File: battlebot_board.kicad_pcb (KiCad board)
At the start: 4 copper layers, 60 x 45 mm, 41 parts, among them J1 Conn_01x02_Pin, J2 Conn_01x04_Pin, J3 JST_SMD_1.0mm_Vertical, J5 JST_02, J6 JST_02, Q1 AO3400A, Q2 AO3400A, SW1 Switch_Tactile_CnK, U1 AP63203WU, U2 LPC824M201JHI33, U3 TMP102, U4 LSM6DSOX, U5 W25Q128JVP

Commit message: added fuses and moved diodes for thermal protection
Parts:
- removed the Ref** at (177.0, 62.0)
- added F1: 16V/2.5A/5.0A, PCM_SparkFun-Fuse:1812, F.Cu at (179.9, 60.5)
- added F2: 16V/2.5A/5.0A, PCM_SparkFun-Fuse:1812, F.Cu at (175.5, 60.5)
- added F3: 16V/2.5A/5.0A, PCM_SparkFun-Fuse:1812, F.Cu at (171.1, 60.5)
- added Ref**: Val**, PCM_SparkFun-Aesthetic:OSHW_Logo_6mm, F.Cu at (159.0, 73.0)
- moved R1 3.04 mm to (184.0, 88.5)
- moved SW1 3.04 mm to (179.5, 92.0)
- moved D4 1.00 mm to (195.1, 82.0)
- moved D5 1.00 mm to (195.0, 89.5)
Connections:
- C10 pad 1: 12V -> Net-(D4-K)
- C12 pad 1: 12V -> Net-(D4-K)
- D4 pad 1: 12V -> Net-(D4-K)
- D5 pad 1: 12V -> Net-(D4-K)
- J5 pad 2: 12V -> Net-(D4-K)
- J6 pad 2: 12V -> Net-(D4-K)
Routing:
- net Net-(D4-K): track 0.00 -> 58.2 mm, vias 0 -> 5
- net 12V: track 90.7 -> 84.1 mm, vias 2 -> 0
- net /NRST: track 31.5 -> 29.8 mm
- net Net-(D5-A): track 54.6 -> 55.6 mm

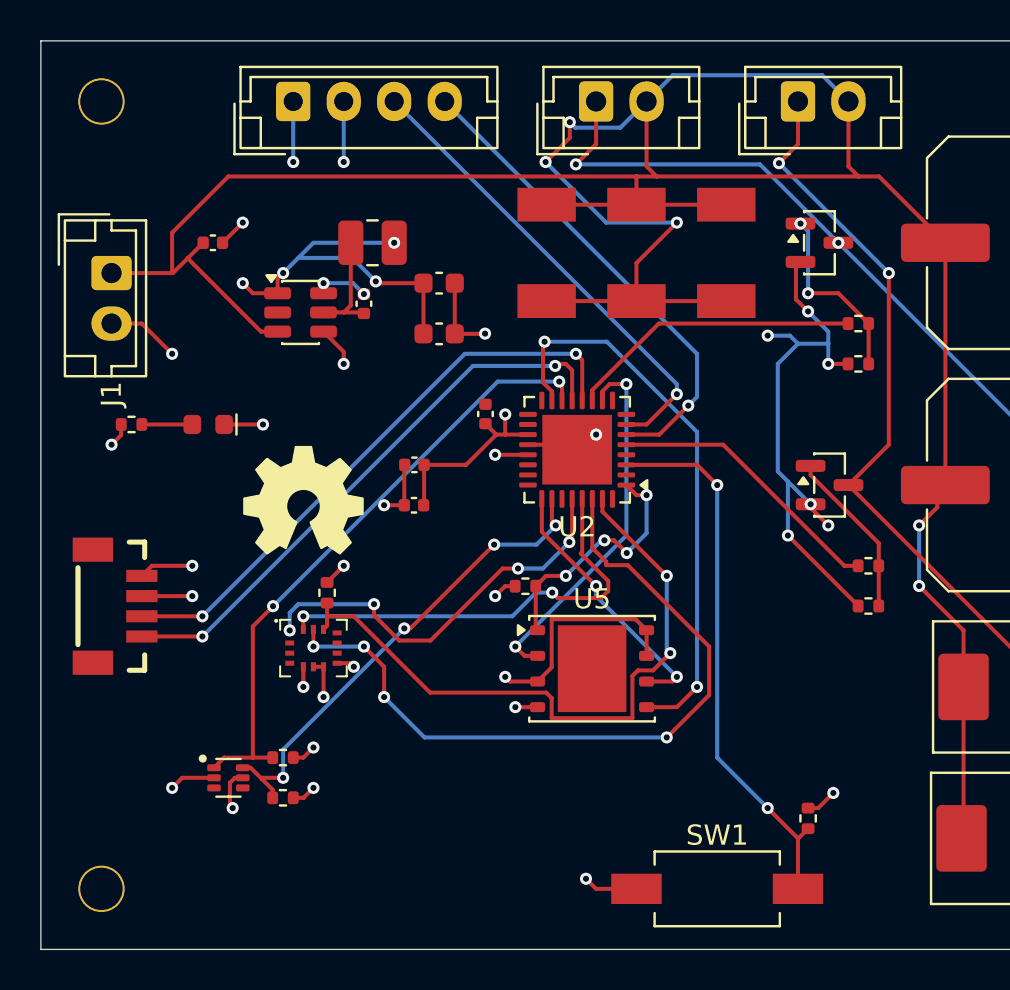
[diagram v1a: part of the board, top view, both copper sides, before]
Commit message: replaced parallel fuses with fuse blade holder
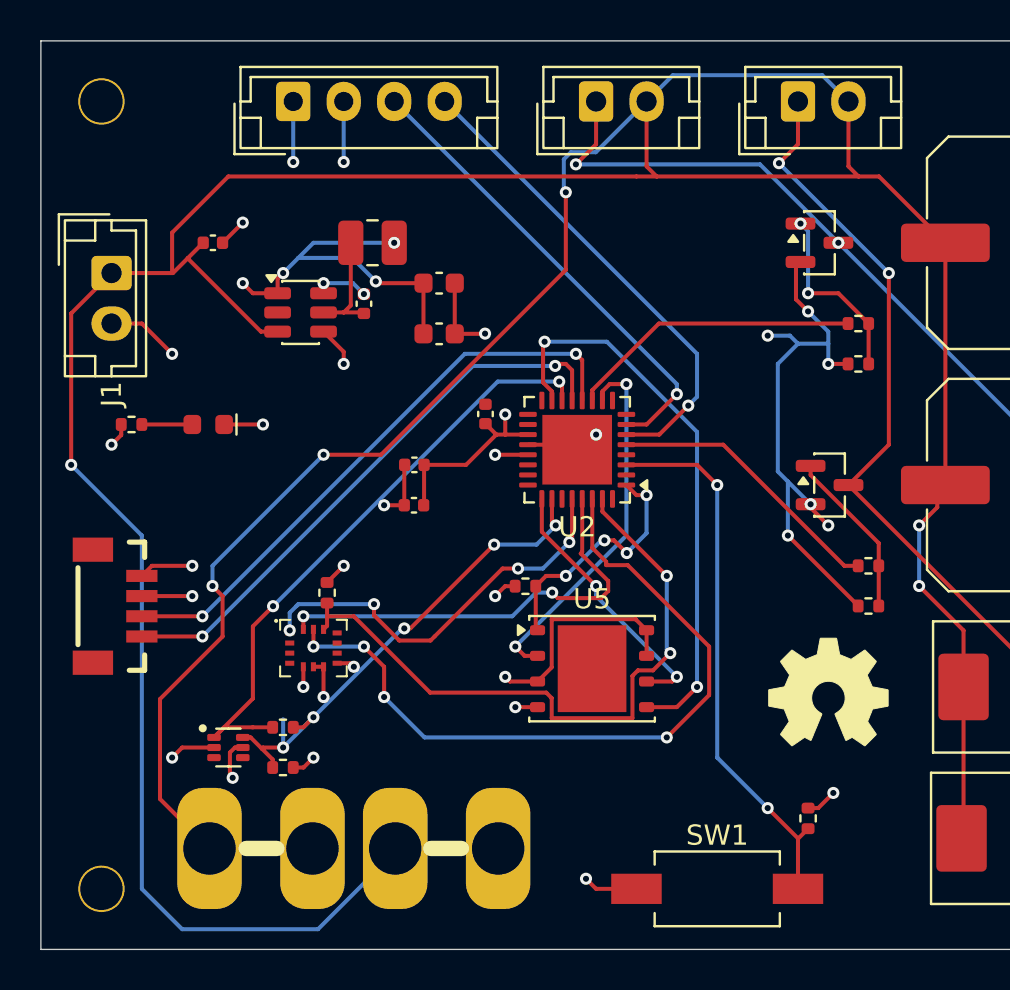
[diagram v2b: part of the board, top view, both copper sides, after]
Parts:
- removed F1, F2, F3: 16V/2.5A/5.0A, PCM_SparkFun-Fuse:1812
- added F4: Blade Fuse, PCM_SparkFun-Fuse:Fuseholder_Automotive, F.Cu at (161.5, 90.0)
- moved Ref** 27.7 mm to (185.0, 82.5)
- moved R4 1.50 mm to (158.0, 84.0)
- moved R5 1.50 mm to (158.0, 86.0)
- moved U3 1.50 mm to (155.3, 85.0)
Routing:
- net 12V: track 84.1 -> 126.8 mm, vias 0 -> 1
- net Net-(D4-K): track 58.2 -> 85.9 mm

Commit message: expose I2C1, fix power delivery wiring, and change credits
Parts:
- added J4: Conn_01x02, Connector_JST:JST_EH_B2B-EH-A_1x02_P2.50mm_Vertical, F.Cu at (148.2, 87.2)
- moved J5 10.0 mm to (183.5, 53.0)
- moved J6 9.50 mm to (174.0, 53.0)
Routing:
- net 12V: track 126.8 -> 64.1 mm
- net Net-(D4-K): track 85.9 -> 106.9 mm
- net Net-(D5-A): track 55.6 -> 45.2 mm, vias 3 -> 2
- net /SCL1: track 30.6 -> 40.8 mm, vias 2 -> 4
- net /SDA1: track 24.3 -> 34.3 mm, vias 4 -> 5
- net Net-(D4-A): track 39.2 -> 45.9 mm, vias 2 -> 3
- net GND: track 70.5 -> 71.6 mm, vias 21 -> 22
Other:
- board text added: "Designed by Benjamin Liu"
- board text removed: "Designed by Benjamin Liu With help from Leo Nguyen"

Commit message: logos and housekeeping
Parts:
- added G***: LOGO, LOGO, B.Cu at (160.5, 112.0)
- moved C2 41.4 mm to (127.0, 91.0)
- moved R10 41.4 mm to (123.0, 100.0)
- moved C1 41.4 mm to (137.0, 102.0)
- moved C10 41.4 mm to (167.7, 91.0)
- moved C12 41.4 mm to (167.7, 103.0)
- moved C4 41.4 mm to (138.2, 93.0)
- moved C5 41.4 mm to (138.2, 95.5)
- moved C7 41.4 mm to (140.5, 99.5)
- moved C8 41.4 mm to (137.0, 104.0)
- moved D3 41.4 mm to (126.8, 100.0)
- moved D4 41.4 mm to (167.6, 113.0)
- moved D5 41.4 mm to (167.5, 120.5)
- moved F4 41.4 mm to (134.0, 121.0)
- moved H1 41.4 mm to (121.5, 84.0)
- moved H2 41.4 mm to (175.5, 84.0)
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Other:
- board text added: "SDA SCL"

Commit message: fixes
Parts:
- moved J3 2.55 mm to (121.5, 106.5)
- moved J4 1.76 mm to (120.5, 116.5)
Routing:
- net 3.3V: track 57.8 -> 53.7 mm
- net 12V: track 64.1 -> 66.1 mm
- net Net-(D4-A): track 45.9 -> 47.2 mm, vias 3 -> 5
- net /SDA1: track 34.3 -> 35.4 mm
- net /SCL1: track 40.8 -> 40.1 mm
- net /TXD: track 28.5 -> 28.0 mm
- net /RXD: track 29.3 -> 28.8 mm

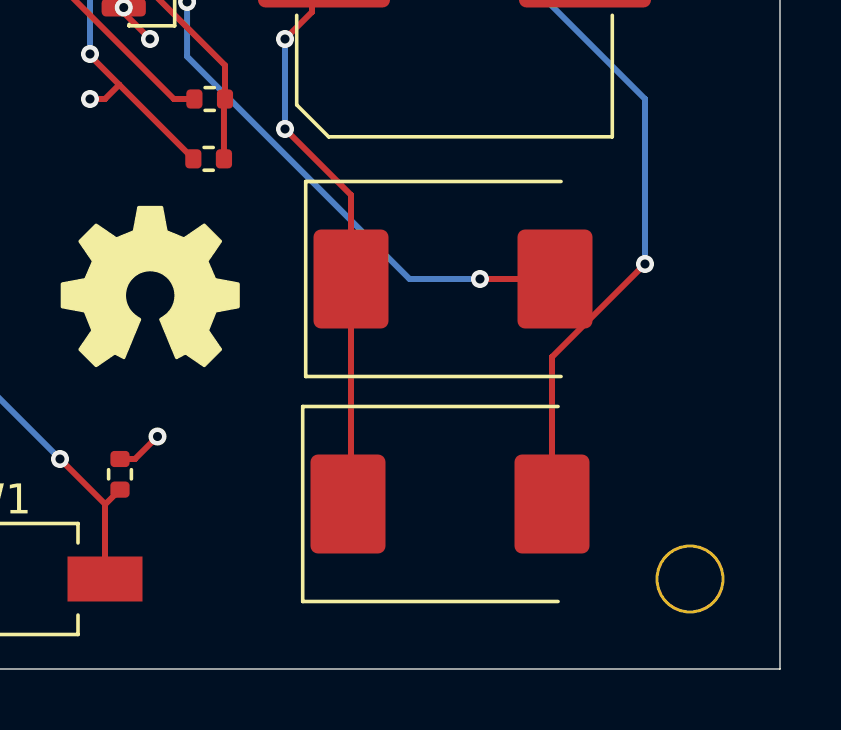
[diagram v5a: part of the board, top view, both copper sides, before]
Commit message: stitching vias
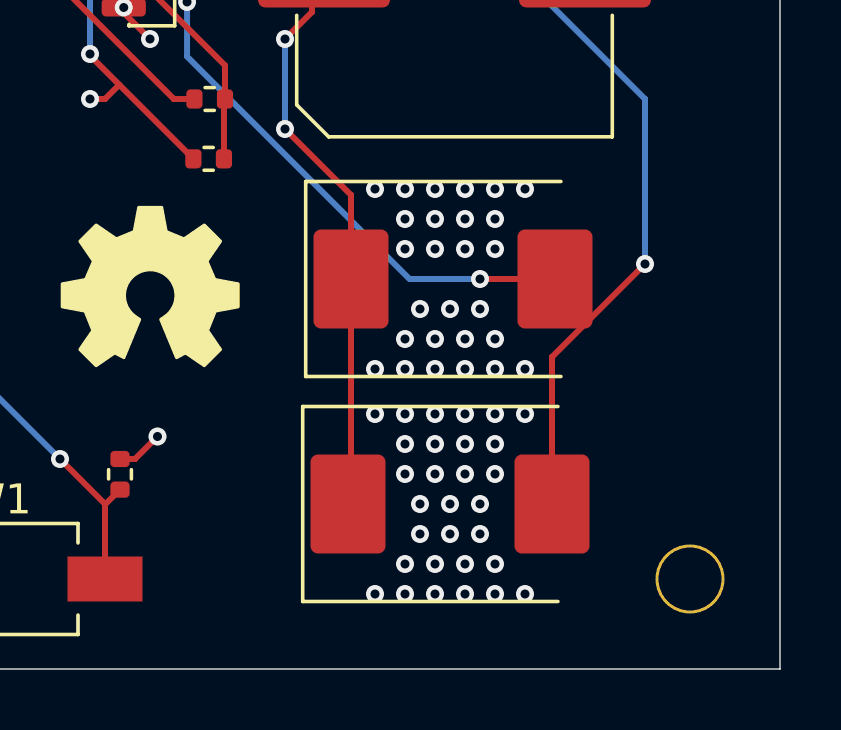
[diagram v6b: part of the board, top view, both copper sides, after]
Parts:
- moved G*** 5.52 mm to (155.0, 111.5)
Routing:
- net (no net): vias 0 -> 57

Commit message: redesign
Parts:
- removed D3: Green, PCM_SparkFun-LED:LED_0603_1608Metric_Green
- removed D4, D5: B340, Diode_SMD:D_SMC
- removed F4: Blade Fuse, PCM_SparkFun-Fuse:Fuseholder_Automotive
- removed G***: LOGO, LOGO
- removed H1, H2, H3, H4: ~, PCM_fab:MountingHole_M2
- removed Q1, Q2: AO3400A, Package_TO_SOT_SMD:SOT-23
- removed R10, R7, R9: 10k, PCM_SparkFun-Resistor:R_0402_1005Metric
- removed R8: 100, PCM_SparkFun-Resistor:R_0402_1005Metric
- removed Ref**: Val**, PCM_SparkFun-Aesthetic:OSHW_Logo_6mm
- removed SW1: Switch_Tactile_CnK, PCM_fab:Button_CnK_PTS636.0_6x3.5mm
- added C11: 0.1uF, PCM_SparkFun-Capacitor:C_0402_1005Metric, F.Cu at (146.5, 97.0)
- added C13: 470uF, PCM_SparkFun-Capacitor:Electrolytic_10.3x10.3mm, F.Cu at (177.2, 100.0)
- added C14: 0.1uF, PCM_SparkFun-Capacitor:C_0402_1005Metric, F.Cu at (155.3, 114.0)
- added C15: 1.0uF, PCM_SparkFun-Capacitor:C_0402_1005Metric, F.Cu at (147.1, 116.5)
- added C6: 0.1uF, PCM_SparkFun-Capacitor:C_0402_1005Metric, F.Cu at (162.0, 99.2)
- added C9: 10nF, PCM_SparkFun-Capacitor:C_0402_1005Metric, F.Cu at (162.2, 103.5)
- added D1: Green, PCM_SparkFun-LED:LED_0603_1608Metric_Green, F.Cu at (128.3, 105.6)
- added D2: PMEG4005EJ, Diode_SMD:D_SOD-323F, F.Cu at (148.0, 114.7)
- added F1: 16V/2.5A/5.0A, PCM_SparkFun-Fuse:1812, F.Cu at (139.0, 76.8)
- added J7: Conn_02x03, Connector_PinHeader_1.27mm:PinHeader_2x03_P1.27mm_Vertical, F.Cu at (137.2, 115.9)
- added L2: 600 Ohm, PCM_SparkFun-Capacitor:C_0805_2012Metric, F.Cu at (159.0, 104.2)
- added L3: 10uH, PCM_SparkFun-Capacitor:C_0805_2012Metric, F.Cu at (151.5, 113.2)
- added REF**: MountingHole_2.2mm_M2_DIN965, MountingHole:MountingHole_2.2mm_M2_DIN965, F.Cu at (128.2, 115.2)
- added REF**: MountingHole_2.2mm_M2_DIN965, MountingHole:MountingHole_2.2mm_M2_DIN965, F.Cu at (181.8, 76.8)
- added REF**: MountingHole_2.2mm_M2_DIN965, MountingHole:MountingHole_2.2mm_M2_DIN965, F.Cu at (181.8, 115.2)
- added REF**: MountingHole_2.2mm_M2_DIN965, MountingHole:MountingHole_2.2mm_M2_DIN965, F.Cu at (128.2, 76.8)
- C1, C2: value 10uF -> 0.1uF
- C10: value 470uF -> 0.1uF; footprint PCM_SparkFun-Capacitor:Electrolytic_10.3x10.3mm -> PCM_SparkFun-Capacitor:C_0402_1005Metric
- C3: value 0.1uF -> 22uF; footprint PCM_SparkFun-Capacitor:C_0402_1005Metric -> PCM_SparkFun-Capacitor:C_0603_1608Metric
- C5: value 22uF -> 0.1uF; footprint PCM_SparkFun-Capacitor:C_0603_1608Metric -> PCM_SparkFun-Capacitor:C_0402_1005Metric
- C7: value 0.1uF -> 10uF
- C8: value 0.1uF -> 1.0uF
- J1: value Conn_01x02_Pin -> Conn_01x03_Socket; footprint Connector_JST:JST_EH_B2B-EH-A_1x02_P2.50mm_Vertical -> PCM_SparkFun-Connector:JST_1x03_P1.0mm_Vertical_SMD
- J2: value Conn_01x04_Pin -> Barrel_Jack_SMD; footprint Connector_JST:JST_EH_B4B-EH-A_1x04_P2.50mm_Vertical -> PCM_SparkFun-Connector:Barrel_Jack_SMD
- J3: value JST_SMD_1.0mm_Vertical -> Conn_01x03_Socket; footprint PCM_SparkFun-Connector:JST_1x04_P1.0mm_Vertical_SMD -> PCM_SparkFun-Connector:JST_1x03_P1.0mm_Vertical_SMD
- J4: value Conn_01x02 -> Conn_01x04_Pin; footprint Connector_JST:JST_EH_B2B-EH-A_1x02_P2.50mm_Vertical -> Connector_PinHeader_1.27mm:PinHeader_1x04_P1.27mm_Vertical
- J5: value JST_02 -> Conn_01x04_Socket; footprint Connector_JST:JST_EH_B2B-EH-A_1x02_P2.50mm_Vertical -> PCM_SparkFun-Connector:JST_1x04_P1.0mm_Vertical_SMD
- J6: value JST_02 -> Conn_01x02_Pin; footprint Connector_JST:JST_EH_B2B-EH-A_1x02_P2.50mm_Vertical -> Connector_PinHeader_1.27mm:PinHeader_1x02_P1.27mm_Vertical
- R4, R5: value 4.7k -> 100k
- R6: value 100 -> 33k
- U2: value LPC824M201JHI33 -> LSM6DSOX; footprint Package_DFN_QFN:QFN-32-1EP_5x5mm_P0.5mm_EP3.45x3.45mm -> PCM_SparkFun-Sensor:ST_LGA-14L_2.5x3.0mm_P0.5mm_4x3
- U3: value TMP102 -> W25Q128JVP; footprint PCM_SparkFun-Semiconductor-Standard:SOT-563 -> Package_SON:WSON-8-1EP_6x5mm_P1.27mm_EP3.4x4.3mm
- U4: value LSM6DSOX -> STM32G4A1KEUx; footprint PCM_SparkFun-Sensor:ST_LGA-14L_2.5x3.0mm_P0.5mm_4x3 -> Package_DFN_QFN:QFN-32-1EP_5x5mm_P0.5mm_EP3.45x3.45mm
- U5: value W25Q128JVP -> AP3012; footprint Package_SON:WSON-8-1EP_6x5mm_P1.27mm_EP3.4x4.3mm -> PCM_SparkFun-Semiconductor-Standard:SOT23-5
- moved J4 49.6 mm to (170.1, 115.2)
- moved J1 44.2 mm to (162.0, 73.7), turned to 0 degrees
- moved J3 43.7 mm to (150.5, 73.7), turned to 0 degrees
- moved J5 32.0 mm to (161.7, 115.5), turned to 180 degrees
- moved U4 27.6 mm to (156.6, 98.6)
- moved R4 25.3 mm to (155.8, 116.2), turned to 90 degrees
- moved J6 25.2 mm to (128.3, 101.4)
- moved C2 24.0 mm to (150.5, 86.0), turned to -90 degrees
- moved C8 23.8 mm to (160.8, 103.5), turned to -90 degrees
- moved R1 22.2 mm to (152.3, 97.8), turned to 180 degrees
- moved U3 20.8 mm to (142.3, 101.2)
- moved C7 20.3 mm to (160.8, 100.2), turned to 0 degrees
- moved C1 19.8 mm to (145.3, 84.1), turned to 0 degrees
- moved R6 19.4 mm to (148.3, 111.2), turned to 180 degrees
- moved C12 19.3 mm to (177.2, 86.2)
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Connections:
- C1 pad 1: 3.3V -> VIN
- C10 pad 1: Net-(D4-K) -> /NRST
- C12 pad 1: Net-(D4-K) -> VIN
- C2 pad 1: 12V -> Net-(U1-BST)
- C2 pad 2: GND -> Net-(U1-SW)
- C3 pad 1: Net-(U1-BST) -> 3.3V
- C3 pad 2: Net-(U1-SW) -> GND
- C7 pad 1: GND -> 3.3V
- C7 pad 2: 3.3V -> GND
- C8 pad 1: GND -> Net-(U4-VDDA)
- C8 pad 2: 3.3V -> GND
- J1 pad 1: 12V -> /CH1
- J1 pad 2: GND -> VIN
- J3 pad 1: /TXD -> /CH2
- J3 pad 2: /RXD -> VIN
- J3 pad 3: 3.3V -> GND
- J4 pad 1: /SDA1 -> 3.3V
- J4 pad 2: /SCL1 -> /SWDIO
- J5 pad 1: Net-(D5-A) -> /TX2
- J5 pad 2: Net-(D4-K) -> /RX2
- J6 pad 1: Net-(D4-A) -> 3.3V
- J6 pad 2: Net-(D4-K) -> Net-(D1-A)
- R2 pad 1: /CS1 -> GND
- R2 pad 2: 3.3V -> /BOOT0
- R4 pad 1: /SCL1 -> Net-(U5-~{SHDN})
- R5 pad 1: /SDA1 -> Net-(U5-FB)
- R5 pad 2: 3.3V -> 5V
- R6 pad 1: /MOTOR1 -> GND
- R6 pad 2: Net-(Q1-G) -> Net-(U5-FB)
- U1 pad 2: unconnected-(U1-EN-Pad2) -> VIN
- U1 pad 3: 12V -> VIN
- U2 pad 1: /CS1 -> /MISO
- U2 pad 10: /MISO1 -> unconnected-(U2-OCS_Aux-Pad10)
- U2 pad 11: /MOTOR1 -> unconnected-(U2-SDO_Aux-Pad11)
- U2 pad 12: /RXD -> /CS
- U2 pad 13: /TXD -> /SCK
- U2 pad 14: /SCL1 -> /MOSI
- U2 pad 3: /NRST -> unconnected-(U2-SCx-Pad3)
- U2 pad 5: /MOTOR2 -> 3.3V
- U2 pad 6: /SWCLK -> GND
- U2 pad 7: /SWDIO -> GND
- U2 pad 8: unconnected-(U2-PIO0_11-Pad8) -> 3.3V
- U3 pad 1: /SCL1 -> /CS2
- U3 pad 2: GND -> /MISO2
- U3 pad 3: unconnected-(U3-ALERT-Pad3) -> 3.3V
- U3 pad 4: unconnected-(U3-ADD0-Pad4) -> GND
- U3 pad 5: 3.3V -> /MOSI2
- U3 pad 6: /SDA1 -> /SCK2
- U4 pad 1: /MISO2 -> 3.3V
- U4 pad 10: unconnected-(U4-OCS_Aux-Pad10) -> /SCK
- U4 pad 11: unconnected-(U4-SDO_Aux-Pad11) -> /MISO
- U4 pad 12: /CS2 -> /MOSI
- U4 pad 13: /SCK2 -> unconnected-(U4-PB0-Pad13)
- U4 pad 14: /MOSI2 -> GND
- U4 pad 4: unconnected-(U4-INT1-Pad4) -> /NRST
- U4 pad 5: 3.3V -> unconnected-(U4-PA0-Pad5)
- U4 pad 6: GND -> unconnected-(U4-PA1-Pad6)
- U4 pad 7: GND -> /TX2
- U4 pad 8: 3.3V -> /RX2
- U4 pad 9: unconnected-(U4-INT2-Pad9) -> /CS
- U5 pad 1: /CS1 -> Net-(D2-A)
- U5 pad 2: /MISO1 -> GND
- U5 pad 3: 3.3V -> Net-(U5-FB)
- U5 pad 4: GND -> Net-(U5-~{SHDN})
- U5 pad 5: /MOSI1 -> 3.3V
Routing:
- net Net-(D4-K): track 106.9 -> 0.00 mm, vias 5 -> 0
- net VIN: track 0.00 -> 84.4 mm
- net 12V: track 66.1 -> 0.00 mm, vias 1 -> 0
- net Net-(D4-A): track 47.2 -> 0.00 mm, vias 5 -> 0
- net Net-(D5-A): track 45.2 -> 0.00 mm, vias 2 -> 0
- net /SCL1: track 40.1 -> 0.00 mm, vias 4 -> 0
- net 5V: track 0.00 -> 38.7 mm, vias 0 -> 3
- net /SDA1: track 35.4 -> 0.00 mm, vias 5 -> 0
- net /RXD: track 28.8 -> 0.00 mm, vias 2 -> 0
- net /MOSI1: track 28.1 -> 0.00 mm, vias 2 -> 0
- net /TXD: track 28.0 -> 0.00 mm, vias 2 -> 0
- net /CH2: track 0.00 -> 27.6 mm, vias 0 -> 2
- net /NRST: track 29.8 -> 2.55 mm, vias 2 -> 0
- net /CH1: track 0.00 -> 23.9 mm, vias 0 -> 2
- net /TX2: track 0.00 -> 20.2 mm, vias 0 -> 2
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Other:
- board text added: "40A RESETTABLE"
- board text added: "G V RX TX"
- board text added: "LED1"
- board text added: "S V G"
- board text added: "V G"
- board text added: "V IO CLK GND"
- board text added: "WARNING: CARCINOGEN EXPOSURE"
- board text added: "WARNING: UNFUSED 500mA MAX"
- board text removed: "Antweight Controller V1"
- board text removed: "Designed by Benjamin Liu"
- board text removed: "GND 12V"
- board text removed: "SDA SCL"
- board text removed: "T R V G"
- board text removed: "V G SWDIO SWCLK"

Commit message: redesign udpate
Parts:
- added C16: 0.1uF, PCM_SparkFun-Capacitor:C_0402_1005Metric, F.Cu at (161.0, 92.5)
- added C17: 0.1uF, PCM_SparkFun-Capacitor:C_0402_1005Metric, F.Cu at (167.0, 95.0)
- added F2: 6V/0.5A/1A, PCM_SparkFun-Fuse:0805, F.Cu at (141.5, 115.0)
- added F3: 6V/0.5A/1A, PCM_SparkFun-Fuse:0805, F.Cu at (142.0, 82.0)
- added J8: Socket_01x02, Connector_PinHeader_1.27mm:PinHeader_1x02_P1.27mm_Vertical, F.Cu at (170.2, 76.4)
- added J9: Conn_01x02_Pin, Connector_PinHeader_1.27mm:PinHeader_1x02_P1.27mm_Vertical, F.Cu at (165.2, 76.5)
- added R7: 10, PCM_SparkFun-Resistor:R_0402_1005Metric, F.Cu at (166.4, 80.9)
- added R8: 100, PCM_SparkFun-Resistor:R_0402_1005Metric, F.Cu at (166.4, 79.9)
- added R9: 10, PCM_SparkFun-Resistor:R_0402_1005Metric, F.Cu at (167.5, 82.5)
- added Ref**: Val**, PCM_SparkFun-Aesthetic:OSHW_Logo_6mm, F.Cu at (135.0, 107.0)
- added U6: MCP2562-E-MF, Package_DFN_QFN:DFN-8-1EP_3x3mm_P0.65mm_EP1.55x2.4mm, F.Cu at (165.1, 91.9)
- added U7: BD1020HFV, Package_TO_SOT_SMD:HVSOF5, F.Cu at (165.1, 108.3)
- moved J7 3.44 mm to (133.7, 115.8)
- moved J1 2.50 mm to (159.5, 73.7)
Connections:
- C1 pad 1: VIN -> Net-(U1-EN)
- J7 pad 1: 5V -> Net-(F2-Pad2)
- J7 pad 3: 5V -> Net-(F2-Pad2)
- J7 pad 5: 5V -> Net-(F2-Pad2)
- U1 pad 2: VIN -> Net-(U1-EN)
- U1 pad 3: VIN -> Net-(U1-EN)
- U4 pad 21: unconnected-(U4-PA11-Pad21) -> /CAN_RX
- U4 pad 22: unconnected-(U4-PA12-Pad22) -> /CAN_TX
- U4 pad 5: unconnected-(U4-PA0-Pad5) -> /ADC
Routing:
- net 5V: track 38.7 -> 69.3 mm, vias 3 -> 5
- net Net-(J8-Pin_2): track 0.00 -> 24.0 mm, vias 0 -> 3
- net Net-(J9-Pin_1): track 0.00 -> 22.9 mm, vias 0 -> 3
- net /ADC: track 0.00 -> 21.2 mm, vias 0 -> 2
- net /CAN_TX: track 0.00 -> 11.0 mm, vias 0 -> 2
- net Net-(U1-EN): track 0.00 -> 9.04 mm
- net /CAN_RX: track 0.00 -> 8.13 mm, vias 0 -> 2
- net Net-(F2-Pad2): track 0.00 -> 7.19 mm
- net GND: track 70.7 -> 77.7 mm, vias 24 -> 29
- net Net-(J8-Pin_1): track 0.00 -> 5.76 mm, vias 0 -> 2
- net VIN: track 84.4 -> 79.4 mm
- net 3.3V: track 39.7 -> 42.4 mm, vias 17 -> 18
- net Net-(R7-Pad1): track 0.00 -> 1.28 mm
- net /CH1: track 23.9 -> 24.9 mm
- net Net-(R7-Pad2): track 0.00 -> 1.00 mm
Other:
- board text added: "1A 5V"
- board text added: "1A BUCK"
- board text added: "40A MOTOR"
- board text added: "CAN"
- board text added: "CAN_BT"
- board text added: "CH1"
- board text added: "CH2"
- board text added: "H L"
- board text added: "IMU"
- board text added: "MCU"
- board text added: "MEMORY"
- board text added: "TSNS"
- board text added: "WARNING: 500mA MAX"
- board text removed: "40A RESETTABLE"
- board text removed: "WARNING: UNFUSED 500mA MAX"
